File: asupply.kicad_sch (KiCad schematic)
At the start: 73 parts

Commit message: analog supply complete
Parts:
- removed C?: 10u, symbol Device:C
- removed FB? (x4): FerriteBead_Small, symbol Device:FerriteBead_Small
- added C? (x6): 100n, symbol Device:C
- added C? (x8): 10u, symbol Device:C
- added FB? (x7): 1K@100MHz, symbol Device:FerriteBead_Small
- added R?: 9k01, symbol Device:R
- added R?: 150k, symbol Device:R
- added U? (x2): LT3042xMSE, Package_SO:MSOP-10-1EP_3x3mm_P0.5mm_EP1.68x1.88mm, symbol Regulator_Linear:LT3042xMSE
- FB?: value FerriteBead_Small -> 1K@100MHz
- L?: value L -> 1u
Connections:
- net +1V8: now also FB?.1
- net +5VA: now also FB?.1
- net +9V: now also FB?.1, FB?.1, FB?.2; no longer C?.2, C?.2, D?.2 (A), U?.10 (EN), U?.9 (VIN)
- net GND: now also C?.2, C?.2, C?.2, C?.2, C?.2, C?.2, C?.2, C?.2, C?.2, C?.2, C?.2, C?.2, C?.2, C?.2, R?.1, R?.1, U?.11 (GND), U?.11 (GND), U?.5 (ILIM), U?.5 (ILIM), U?.8 (GND), U?.8 (GND)
- net -9V: now reaches C?.1, C?.1, D?.1 (K), U?.4 (VOUT)
- net -9V: now also FB?.1
- net at C?.1, C?.1, C?.1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: now also FB?.1
- net at C?.1, C?.1, C?.1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: now also FB?.2 (x2)
- net at C?.1, C?.1, C?.1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: now also FB?.2
- net at C?.1, C?.1, U?.1 (IN)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: now also FB?.2
- new net: C?.1, R?.2, U?.7 (SET) (x2)
- new net: C?.1, C?.1, C?.1, FB?.2, U?.1 (IN), U?.2 (IN), U?.3 (EN/UV), U?.6 (PGFB) (x2)
- new net: C?.2, C?.2, D?.2 (A), FB?.1, U?.10 (EN), U?.9 (VIN)
- new net +15V: C?.1, C?.1, C?.1, U?.10 (OUT), U?.9 (OUTS)
- new net +9VA: C?.1, C?.1, C?.1, U?.10 (OUT), U?.9 (OUTS)
- no-connect marks 5 -> 7
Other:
- moved on the sheet: C?, D?, FB?, L?, R?, U?

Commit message: add USB
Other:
- company: (none) -> M-Labs
- title: (none) -> Kirdy
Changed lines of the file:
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@@
 (kicad_sch (version 20211123) (generator eeschema)
   (paper "A3")
+  (title_block
+    (title "Kirdy")
+    (date "2022-07-03")
+    (rev "r0.1")
+    (company "M-Labs")
+    (comment 1 "Alex Wong Tat Hang")
+  )
   (junction (at 175.26 237.49) (diameter 0) (color 0 0 0 0)
   )

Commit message: complete mcu
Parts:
- gave numbers to parts that had none: 93

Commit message: first draft complete
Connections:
- net GND: now also C47.2, C48.2, U9.11 (MODE), U9.13 (GND), U9.2 (RT)
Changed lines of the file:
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@@
     (pin "2")
+  )
+  (symbol (lib_id "power:PWR_FLAG") (at 175.26 76.2 0) (unit 1)
+    (in_bom yes) (on_board yes) (fields_autoplaced)
+    (property "Reference" "#FLG0106" (id 0) (at 175.26 74.295 0)
+      (effects (font (size 1.27 1.27)) hide)
+    )
+    (property "Value" "PWR_FLAG" (id 1) (at 175.26 71.12 0)
+      (effects (font (size 1.27 1.27)) hide)
+    )
+    (property "Footprint" "" (id 2) (at 175.26 76.2 0)
+      (effects (font (size 1.27 1.27)) hide)
+    )
+    (property "Datasheet" "~" (id 3) (at 175.26 76.2 0)
+      (effects (font (size 1.27 1.27)) hide)
+    )
+    (pin "1")
   )
   (symbol (lib_id "Device:C") (at 148.59 209.55 0) (unit 1)
@@
     (pin "2")
   )
+  (symbol (lib_id "power:PWR_FLAG") (at 175.26 107.95 0) (unit 1)
+    (in_bom yes) (on_board yes) (fields_autoplaced)
+    (property "Reference" "#FLG0108" (id 0) (at 175.26 106.045 0)
+      (effects (font (size 1.27 1.27)) hide)
+    )
+    (property "Value" "PWR_FLAG" (id 1) (at 175.26 102.87 0)
+      (effects (font (size 1.27 1.27)) hide)
+    )
+    (property "Footprint" "" (id 2) (at 175.26 107.95 0)
+      (effects (font (size 1.27 1.27)) hide)
+    )
+    (property "Datasheet" "~" (id 3) (at 175.26 107.95 0)
+      (effects (font (size 1.27 1.27)) hide)
+    )
+    (pin "1")
+  )
   (symbol (lib_id "Device:FerriteBead_Small") (at 73.66 195.58 180) (unit 1)
     (in_bom yes) (on_board yes)
@@
     (pin "2")
   )
+  (symbol (lib_id "power:PWR_FLAG") (at 175.26 138.43 0) (unit 1)
+    (in_bom yes) (on_board yes) (fields_autoplaced)
+    (property "Reference" "#FLG0109" (id 0) (at 175.26 136.525 0)
+      (effects (font (size 1.27 1.27)) hide)
+    )
+    (property "Value" "PWR_FLAG" (id 1) (at 175.26 133.35 0)
+      (effects (font (size 1.27 1.27)) hide)
+    )
+    (property "Footprint" "" (id 2) (at 175.26 138.43 0)
+      (effects (font (size 1.27 1.27)) hide)
+    )
+    (property "Datasheet" "~" (id 3) (at 175.26 138.43 0)
+      (effects (font (size 1.27 1.27)) hide)
+    )
+    (pin "1")
+  )
   (symbol (lib_id "power:GND") (at 281.94 91.44 0) (unit 1)
     (in_bom yes) (on_board yes) (fields_autoplaced)
@@
     )
     (property "Datasheet" "" (id 3) (at 281.94 44.45 0)
+      (effects (font (size 1.27 1.27)) hide)
+    )
+    (pin "1")
+  )
+  (symbol (lib_id "power:PWR_FLAG") (at 185.42 201.93 0) (unit 1)
+    (in_bom yes) (on_board yes) (fields_autoplaced)
+    (property "Reference" "#FLG0102" (id 0) (at 185.42 200.025 0)
+      (effects (font (size 1.27 1.27)) hide)
+    )
+    (property "Value" "PWR_FLAG" (id 1) (at 185.42 196.85 0)
+      (effects (font (size 1.27 1.27)) hide)
+    )
+    (property "Footprint" "" (id 2) (at 185.42 201.93 0)
+      (effects (font (size 1.27 1.27)) hide)
+    )
+    (property "Datasheet" "~" (id 3) (at 185.42 201.93 0)
       (effects (font (size 1.27 1.27)) hide)
     )
@@
     (pin "2")
   )
+  (symbol (lib_id "power:PWR_FLAG") (at 186.69 237.49 0) (unit 1)
+    (in_bom yes) (on_board yes) (fields_autoplaced)
+    (property "Reference" "#FLG0101" (id 0) (at 186.69 235.585 0)
+      (effects (font (size 1.27 1.27)) hide)
+    )
+    (property "Value" "PWR_FLAG" (id 1) (at 186.69 232.41 0)
+      (effects (font (size 1.27 1.27)) hide)
+    )
+    (property "Footprint" "" (id 2) (at 186.69 237.49 0)
+      (effects (font (size 1.27 1.27)) hide)
+    )
+    (property "Datasheet" "~" (id 3) (at 186.69 237.49 0)
+      (effects (font (size 1.27 1.27)) hide)
+    )
+    (pin "1")
+  )
   (symbol (lib_id "Device:R") (at 203.2 113.03 90) (unit 1)
     (in_bom yes) (on_board yes)
@@
     (pin "2")
   )
+  (symbol (lib_id "power:PWR_FLAG") (at 88.9 237.49 0) (unit 1)
+    (in_bom yes) (on_board yes) (fields_autoplaced)
+    (property "Reference" "#FLG0104" (id 0) (at 88.9 235.585 0)
+      (effects (font (size 1.27 1.27)) hide)
+    )
+    (property "Value" "PWR_FLAG" (id 1) (at 88.9 232.41 0)
+      (effects (font (size 1.27 1.27)) hide)
+    )
+    (property "Footprint" "" (id 2) (at 88.9 237.49 0)
+      (effects (font (size 1.27 1.27)) hide)
+    )
+    (property "Datasheet" "~" (id 3) (at 88.9 237.49 0)
+      (effects (font (size 1.27 1.27)) hide)
+    )
+    (pin "1")
+  )
   (symbol (lib_id "Device:C") (at 175.26 146.05 0) (unit 1)
     (in_bom yes) (on_board yes) (fields_autoplaced)
@@
     )
     (property "Datasheet" "" (id 3) (at 146.05 168.91 0)
+      (effects (font (size 1.27 1.27)) hide)
+    )
+    (pin "1")
+  )
+  (symbol (lib_id "power:PWR_FLAG") (at 175.26 168.91 0) (unit 1)
+    (in_bom yes) (on_board yes) (fields_autoplaced)
+    (property "Reference" "#FLG0103" (id 0) (at 175.26 167.005 0)
+      (effects (font (size 1.27 1.27)) hide)
+    )
+    (property "Value" "PWR_FLAG" (id 1) (at 175.26 163.83 0)
+      (effects (font (size 1.27 1.27)) hide)
+    )
+    (property "Footprint" "" (id 2) (at 175.26 168.91 0)
+      (effects (font (size 1.27 1.27)) hide)
+    )
+    (property "Datasheet" "~" (id 3) (at 175.26 168.91 0)
+      (effects (font (size 1.27 1.27)) hide)
+    )
+    (pin "1")
+  )
+  (symbol (lib_id "power:PWR_FLAG") (at 73.66 201.93 90) (unit 1)
+    (in_bom yes) (on_board yes) (fields_autoplaced)
+    (property "Reference" "#FLG0105" (id 0) (at 71.755 201.93 0)
+      (effects (font (size 1.27 1.27)) hide)
+    )
+    (property "Value" "PWR_FLAG" (id 1) (at 68.58 201.93 0)
+      (effects (font (size 1.27 1.27)) hide)
+    )
+    (property "Footprint" "" (id 2) (at 73.66 201.93 0)
+      (effects (font (size 1.27 1.27)) hide)
+    )
+    (property "Datasheet" "~" (id 3) (at 73.66 201.93 0)
       (effects (font (size 1.27 1.27)) hide)
     )
@@
     (pin "2")
   )
+  (symbol (lib_id "power:PWR_FLAG") (at 175.26 44.45 0) (unit 1)
+    (in_bom yes) (on_board yes) (fields_autoplaced)
+    (property "Reference" "#FLG0107" (id 0) (at 175.26 42.545 0)
+      (effects (font (size 1.27 1.27)) hide)
+    )
+    (property "Value" "PWR_FLAG" (id 1) (at 175.26 39.37 0)
+      (effects (font (size 1.27 1.27)) hide)
+    )
+    (property "Footprint" "" (id 2) (at 175.26 44.45 0)
+      (effects (font (size 1.27 1.27)) hide)
+    )
+    (property "Datasheet" "~" (id 3) (at 175.26 44.45 0)
+      (effects (font (size 1.27 1.27)) hide)
+    )
+    (pin "1")
+  )
   (symbol (lib_id "Device:C") (at 124.46 48.26 0) (unit 1)
     (in_bom yes) (on_board yes) (fields_autoplaced)
@@
     (pin "2")
   )
+  (symbol (lib_id "power:GND") (at 135.89 217.17 0) (unit 1)
+    (in_bom yes) (on_board yes) (fields_autoplaced)
+    (property "Reference" "#PWR0160" (id 0) (at 135.89 223.52 0)
+      (effects (font (size 1.27 1.27)) hide)
+    )
+    (property "Value" "GND" (id 1) (at 135.89 222.25 0))
+    (property "Footprint" "" (id 2) (at 135.89 217.17 0)
+      (effects (font (size 1.27 1.27)) hide)
+    )
+    (property "Datasheet" "" (id 3) (at 135.89 217.17 0)
+      (effects (font (size 1.27 1.27)) hide)
+    )
+    (pin "1")
+  )
   (symbol (lib_id "Device:C") (at 55.88 48.26 0) (unit 1)

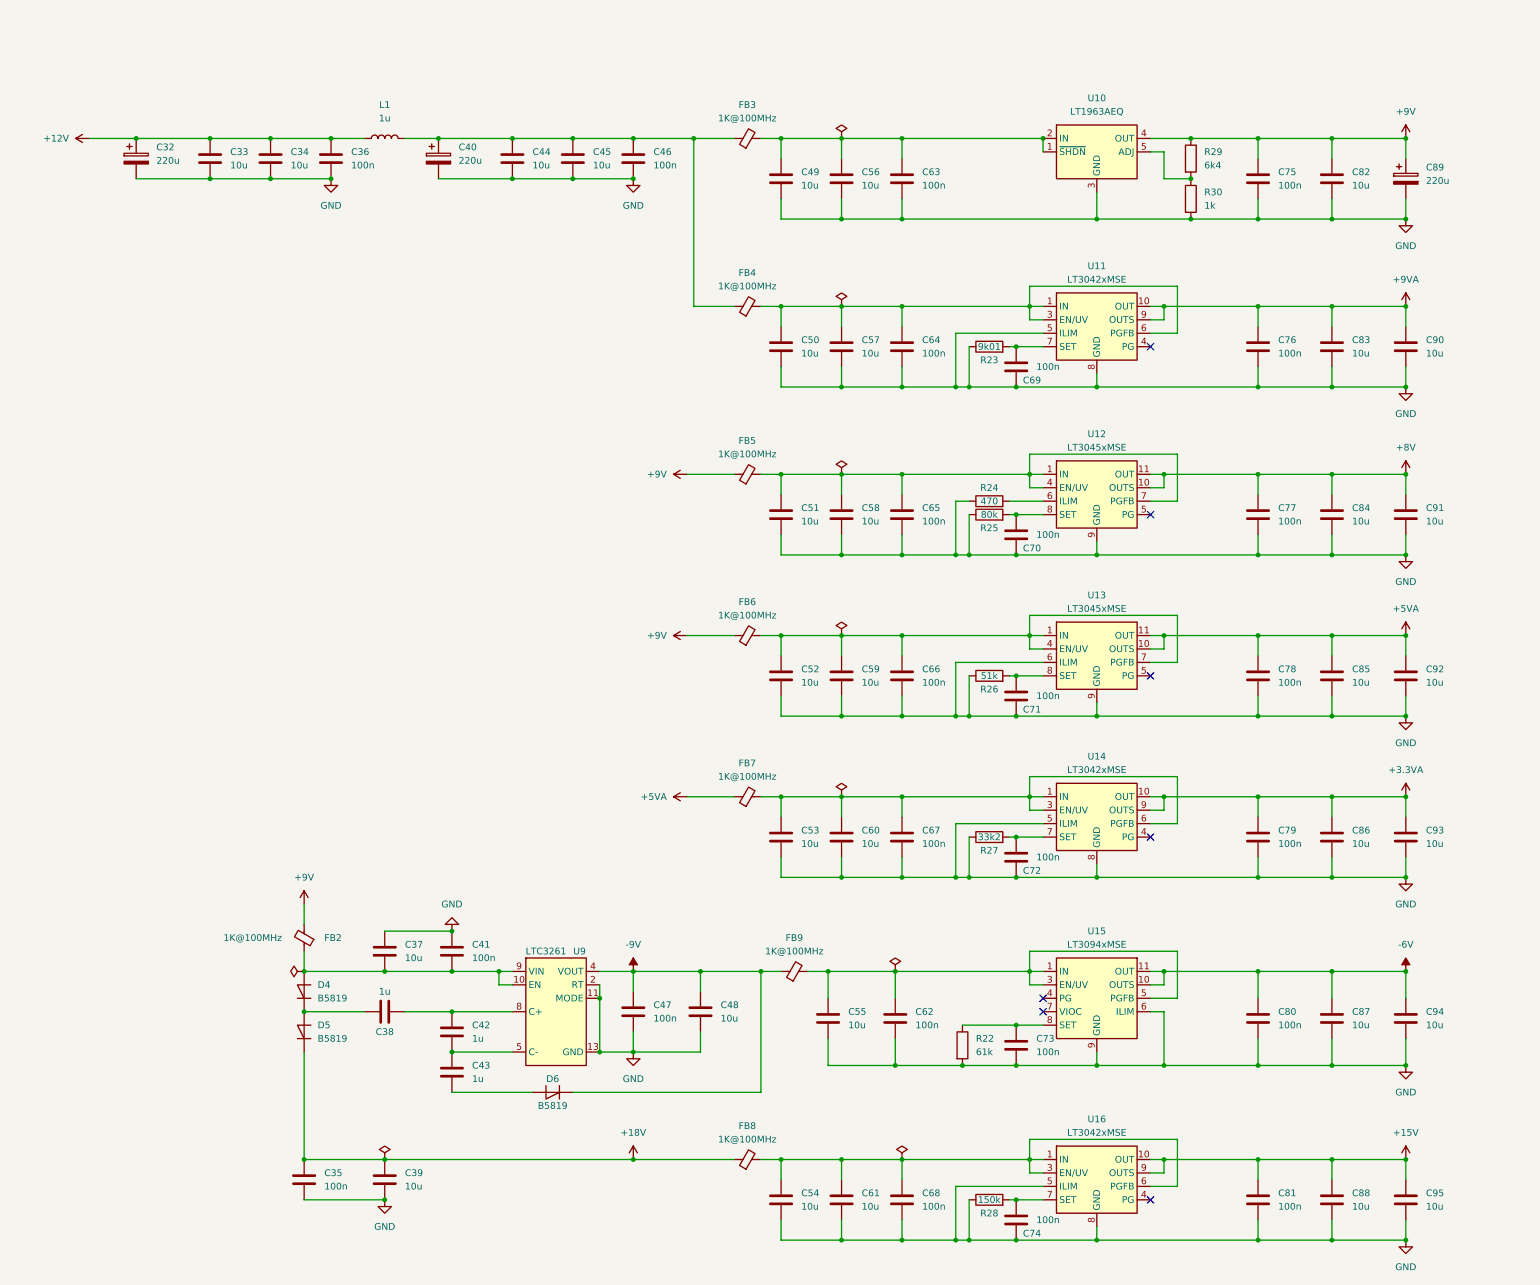
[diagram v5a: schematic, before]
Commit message: Complete BOM, FP assignment
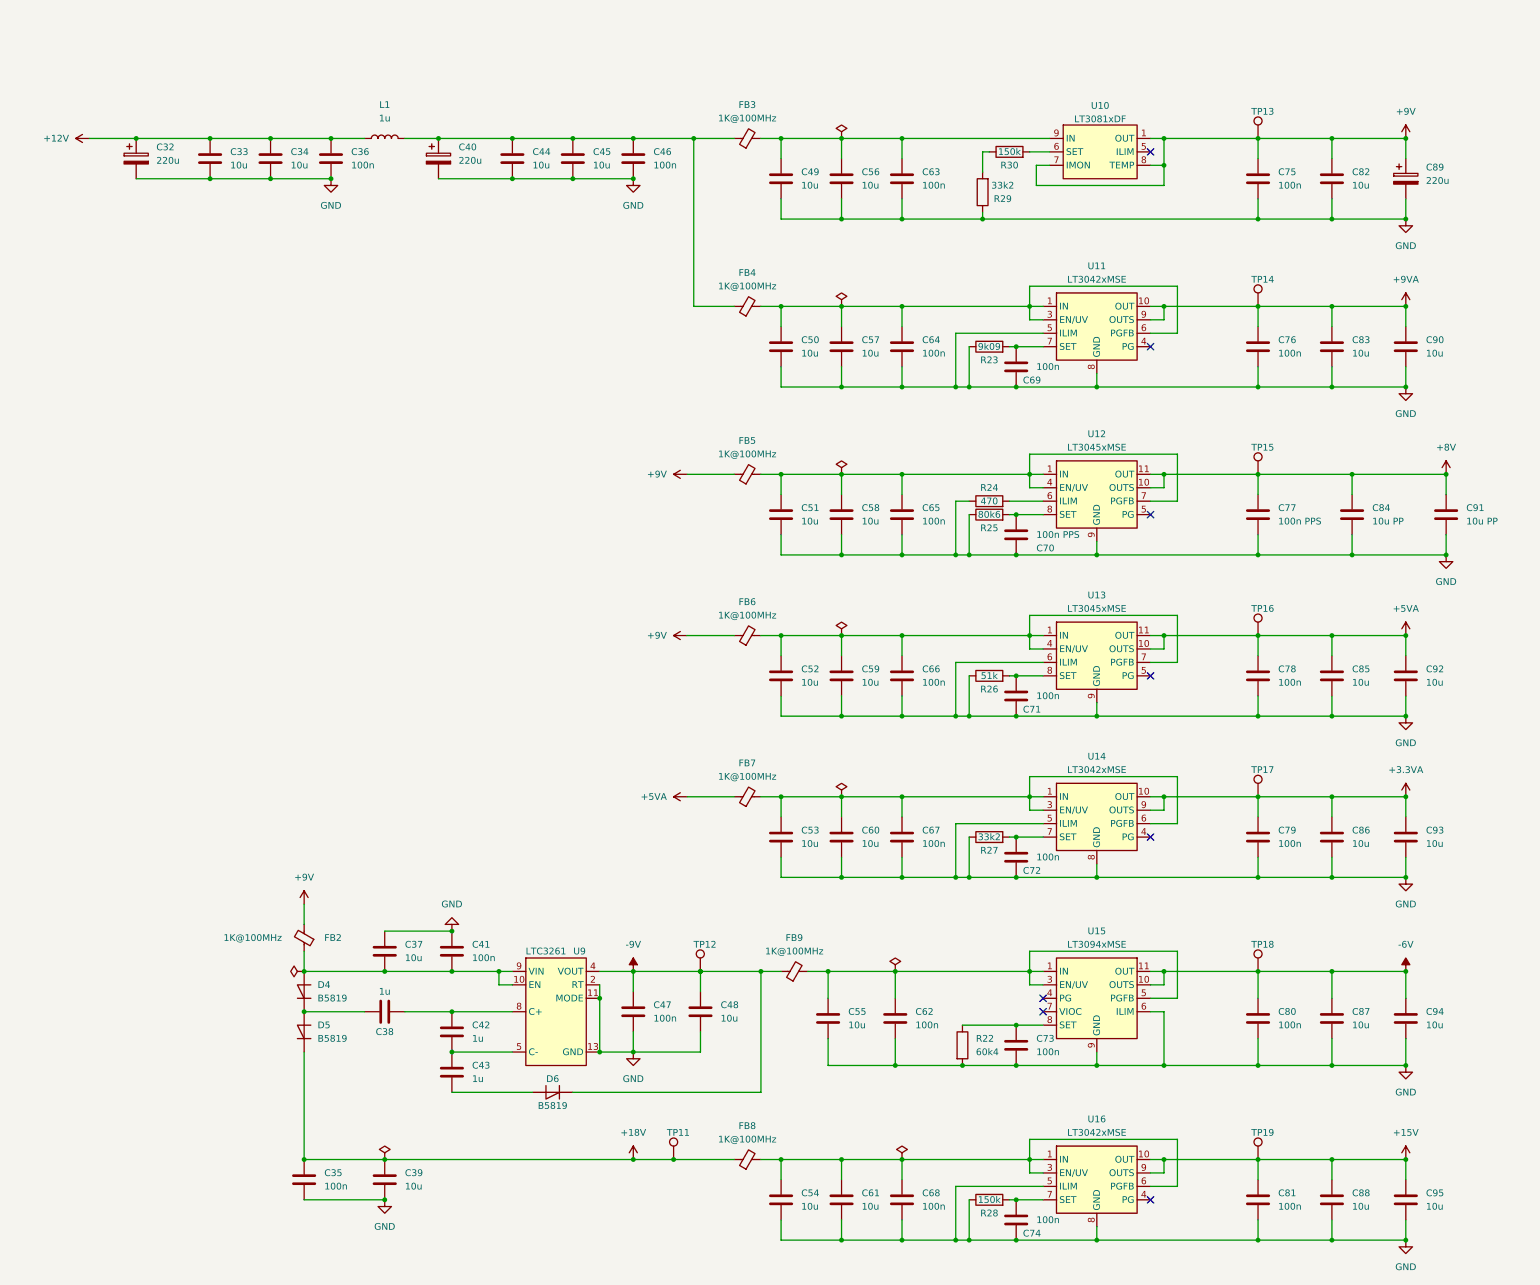
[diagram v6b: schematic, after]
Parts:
- removed U10: LT1963AEQ, Package_TO_SOT_SMD:TO-263-5_TabPin3, symbol Regulator_Linear:LT1963AEQ
- added TP11, TP12, TP13, TP14, TP15, TP16, TP17, TP18, TP19: TestPoint, TestPoint:TestPoint_Pad_2.0x2.0mm, symbol Connector:TestPoint
- added U10: LT3081xDF, Package_DFN_QFN:DFN-12-1EP_4x4mm_P0.5mm_EP2.66x3.38mm, symbol kirdy:LT3081xDF
- C32, C40, C89: footprint (none) -> Capacitor_Tantalum_SMD:CP_EIA-7343-15_Kemet-W; MFR_PN (none) -> T491D227K016AT; MFR_PN_ALT (none) -> 293D227X9016E2TE3
- C33, C34, C37, C39, C44, C45, C48, C49, C50, C51, C52, C53, C54, C55, C56, C57, C58, C59, C60, C61, C82, C83, C85, C86, C87, C88, C90, C92, C93, C94, C95: footprint (none) -> Capacitor_SMD:C_0805_2012Metric; MFR_PN (none) -> CL21B106KOQNNNG; MFR_PN_ALT (none) -> CL21B106KOQNNNE
- C35, C36, C41, C46, C47, C62, C63, C64, C65, C66, C67, C68, C69, C71, C72, C73, C74, C75, C76, C78, C79, C80, C81: footprint (none) -> Capacitor_SMD:C_0603_1608Metric; MFR_PN (none) -> CL10B104KB8NNWC; MFR_PN_ALT (none) -> CL10B104KB8NNNL
- C38, C42, C43: footprint (none) -> Capacitor_SMD:C_0603_1608Metric; MFR_PN (none) -> CL10B105KA8NNNC; MFR_PN_ALT (none) -> CGA3E1X7R1E105K080AC
- C70, C77: value 100n -> 100n PPS; footprint (none) -> Capacitor_SMD:C_1210_3225Metric; MFR_PN (none) -> ECH-U1C104JX5
- C84, C91: value 10u -> 10u PP; footprint (none) -> Capacitor_SMD:C_1812_4532Metric; MFR_PN (none) -> 16MU106MC44532
- D4, D5, D6: footprint (none) -> Diode_SMD:D_SOD-323; MFR_PN (none) -> B5819WS-TP
- FB2, FB3, FB4, FB5, FB6, FB7, FB8, FB9: footprint (none) -> Inductor_SMD:L_1210_3225Metric; MFR_PN (none) -> FBMH3225HM102NT; MFR_PN_ALT (none) -> FBMH3225HM102NTV
- L1: footprint (none) -> Inductor_SMD:L_1008_2520Metric; MFR_PN (none) -> DFE252012F-1R0M=P2; MFR_PN_ALT (none) -> DFE252012P-1R0M=P2
- R22: value 61k -> 60k4; footprint (none) -> Resistor_SMD:R_0603_1608Metric; MFR_PN (none) -> RT0603FRE0760K4L; MFR_PN_ALT (none) -> RC0603FR-0760K4L
- R23: value 9k01 -> 9k09; footprint (none) -> Resistor_SMD:R_0603_1608Metric; MFR_PN (none) -> CR0603-FX-9091ELF; MFR_PN_ALT (none) -> RK73H1JTTD9091F
- R24: footprint (none) -> Resistor_SMD:R_0603_1608Metric; MFR_PN (none) -> WR06X4700FTL; MFR_PN_ALT (none) -> RC0603FR-07470RL
- R25: value 80k -> 80k6; footprint (none) -> Resistor_SMD:R_0603_1608Metric; MFR_PN (none) -> RC0603FR-0780K6L; MFR_PN_ALT (none) -> RK73H1JTTD8062F
- R26: footprint (none) -> Resistor_SMD:R_0603_1608Metric; MFR_PN (none) -> RMCF0603FT51K0; MFR_PN_ALT (none) -> CR0603-FX-5102ELF
- R27: footprint (none) -> Resistor_SMD:R_0603_1608Metric; MFR_PN (none) -> CR0603-FX-3322ELF; MFR_PN_ALT (none) -> RC0603FR-0733K2L
- R28: footprint (none) -> Resistor_SMD:R_0603_1608Metric; MFR_PN (none) -> CRGCQ0603F150K; MFR_PN_ALT (none) -> RMCF0603FG150K
- R29: value 6k4 -> 33k2; footprint (none) -> Resistor_SMD:R_0603_1608Metric; MFR_PN (none) -> CR0603-FX-3322ELF; MFR_PN_ALT (none) -> RC0603FR-0733K2L
- R30: value 1k -> 150k; footprint (none) -> Resistor_SMD:R_0603_1608Metric; MFR_PN (none) -> CRGCQ0603F150K; MFR_PN_ALT (none) -> RMCF0603FG150K
- U11, U14, U16: MFR_PN (none) -> LT3042IMSE#PBF; MFR_PN_ALT (none) -> LT3042IMSE#TRPBF
- U12, U13: MFR_PN (none) -> LT3045EMSE-1#PBF; MFR_PN_ALT (none) -> LT3045IMSE-1#PBF
- U15: MFR_PN (none) -> LT3094IMSE#PBF; MFR_PN_ALT (none) -> LT3094EMSE#PBF
- U9: MFR_PN (none) -> LTC3261IMSE#TRPBF; MFR_PN_ALT (none) -> LTC3261EMSE#TRPBF
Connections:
- net +15V: now also TP19.1
- net +1V8: now also TP11.1
- net +3.3VA: now also TP17.1
- net +5VA: now also TP16.1
- net +8V: now also TP15.1
- net +9V: now also TP13.1, U10.1 (OUT), U10.13 (OUT), U10.2 (OUT), U10.3 (OUT), U10.4 (OUT), U10.7 (IMON), U10.8 (TEMP); no longer R29.1
- net +9VA: now also TP14.1
- net -6V: now also TP18.1
- net -9V: now also TP12.1
- net GND: now also R29.1; no longer R30.2
- net IN: now reaches C49.1, C56.1, C63.1, FB3.2
- net IN: now also U10.10 (IN), U10.11 (IN), U10.12 (IN), U10.9 (IN)
- new net: R30.2, U10.6 (SET)
- no-connect marks 7 -> 8
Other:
- moved on the sheet: C84, C91

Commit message: complete placement
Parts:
- added C173: 100n, Capacitor_SMD:C_0603_1608Metric, symbol Device:C
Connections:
- net GND: now also C173.2
- net at R30.2, U10.6 (SET): now also C173.1
- net +1V8: no longer names the net of C35.1, C39.1, D5.1 (K), FB8.1, TP11.1
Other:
- moved on the sheet: C75, C82, C89, TP13, U10
